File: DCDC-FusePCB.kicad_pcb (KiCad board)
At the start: 2 copper layers, 59 x 39 mm, 11 parts, among them J1 Conn_01x02_Socket, J2 Conn_01x02_Socket

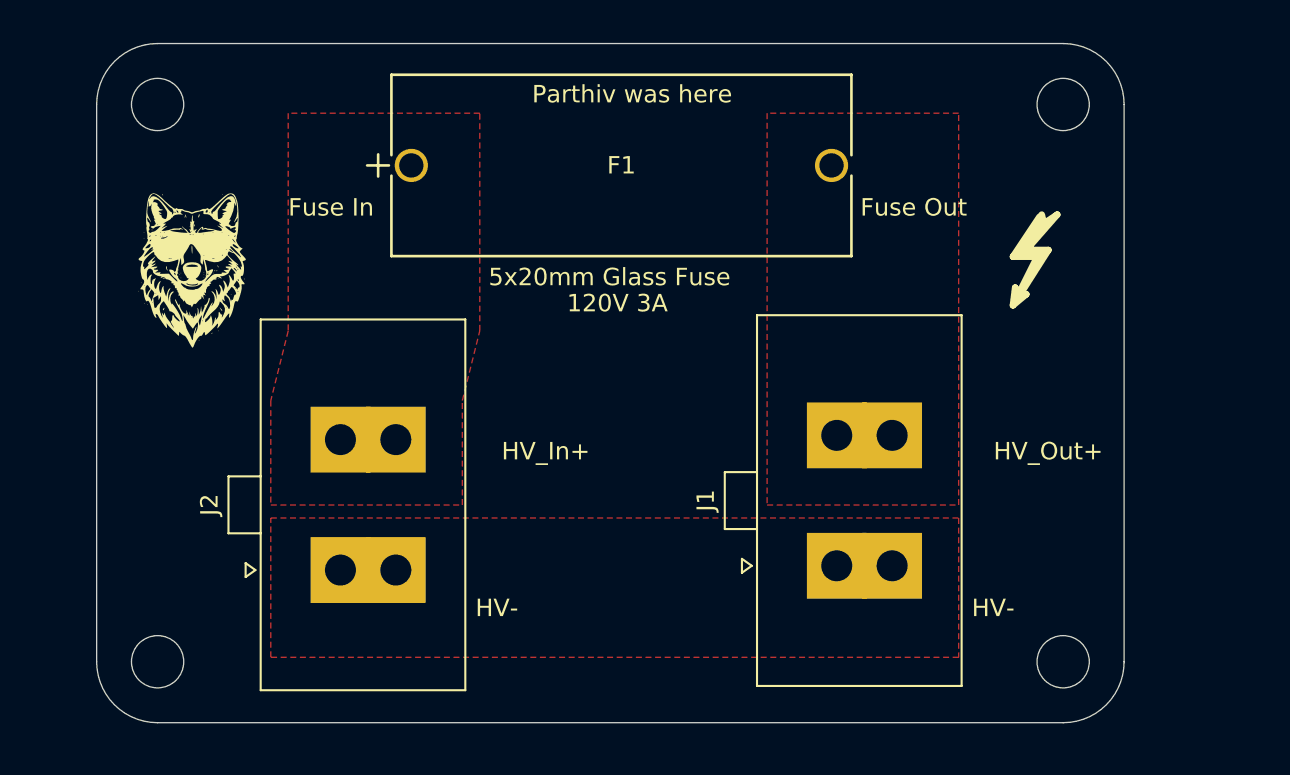
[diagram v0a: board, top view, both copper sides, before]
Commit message: replaced conns with screw terminals
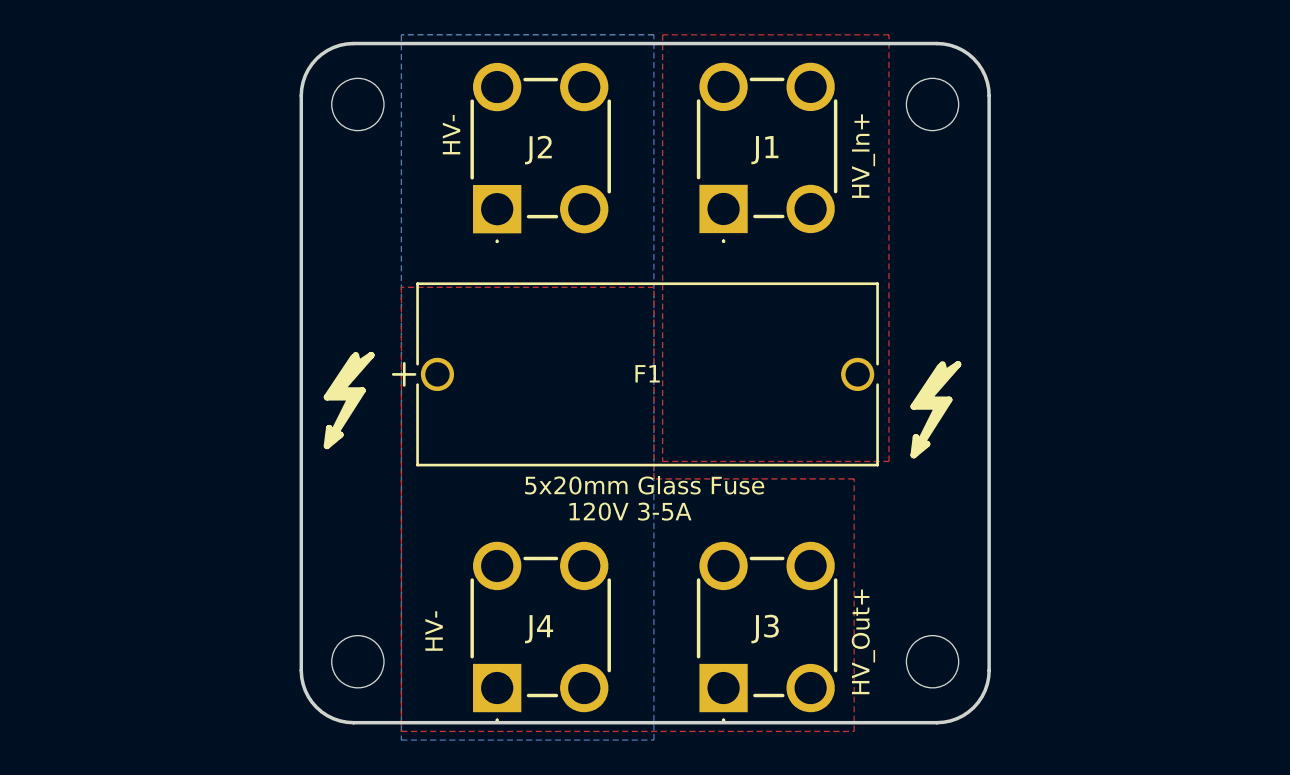
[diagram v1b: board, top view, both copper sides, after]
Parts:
- removed the G*** at (115.0, 80.0)
- added J3: Conn_01x01, CustomFootprints:81915, F.Cu at (145.5, 104.0)
- added J4: Conn_01x01, CustomFootprints:81915, F.Cu at (132.5, 104.0)
- added REF**: Symbol_HighVoltage_Small, UTSVT_Special:Symbol_HighVoltage_Small, F.Cu at (156.8, 88.6)
- J1, J2: value Conn_01x02_Socket -> Conn_01x01; footprint Connector_Molex:Molex_Sabre_43160-0102_1x02_P7.49mm_Vertical -> CustomFootprints:81915
- moved REF** 40.2 mm to (123.1, 88.1)
- moved J1 22.7 mm to (145.5, 76.5), turned to 0 degrees
- moved J2 21.5 mm to (132.5, 76.5), turned to 0 degrees
- moved G*** 20.1 mm to (157.0, 87.0), turned to -90 degrees
- moved F1 12.1 mm to (129.1, 86.0)
- moved REF** 11.5 mm to (124.5, 102.5)
- moved REF** 11.5 mm to (124.5, 70.5)
- moved REF** 7.50 mm to (157.5, 70.5)
- moved REF** 7.50 mm to (157.5, 102.5)
- moved G*** 5.70 mm to (135.5, 86.5)
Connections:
- F1 pad 1: Net-(J2-Pin_2) -> /HV+_Out
- F1 pad 2: Net-(J1-Pin_2) -> /HV+_In
- J1 pad 1: Net-(J1-Pin_1) -> /HV+_In
- J2 pad 1: Net-(J1-Pin_1) -> /HV-
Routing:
- added copper zone on F.Cu, net (none)
- added copper zone on F.Cu, net /HV+_Out
- added copper zone on B.Cu, net /HV-
- removed copper zone on F.Cu, net Net-(J1-Pin_1)
- removed copper zone on F.Cu, net Net-(J1-Pin_2)
- removed copper zone on F.Cu, net Net-(J2-Pin_2)
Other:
- board size 59 x 39 mm -> 39.5 x 39 mm
- board text added: "120V 3-5A"
- board text removed: "120V 3A"
- board text removed: "Fuse In"
- board text removed: "Fuse Out"
- board text removed: "Parthiv was here"

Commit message: mountinghole pads design
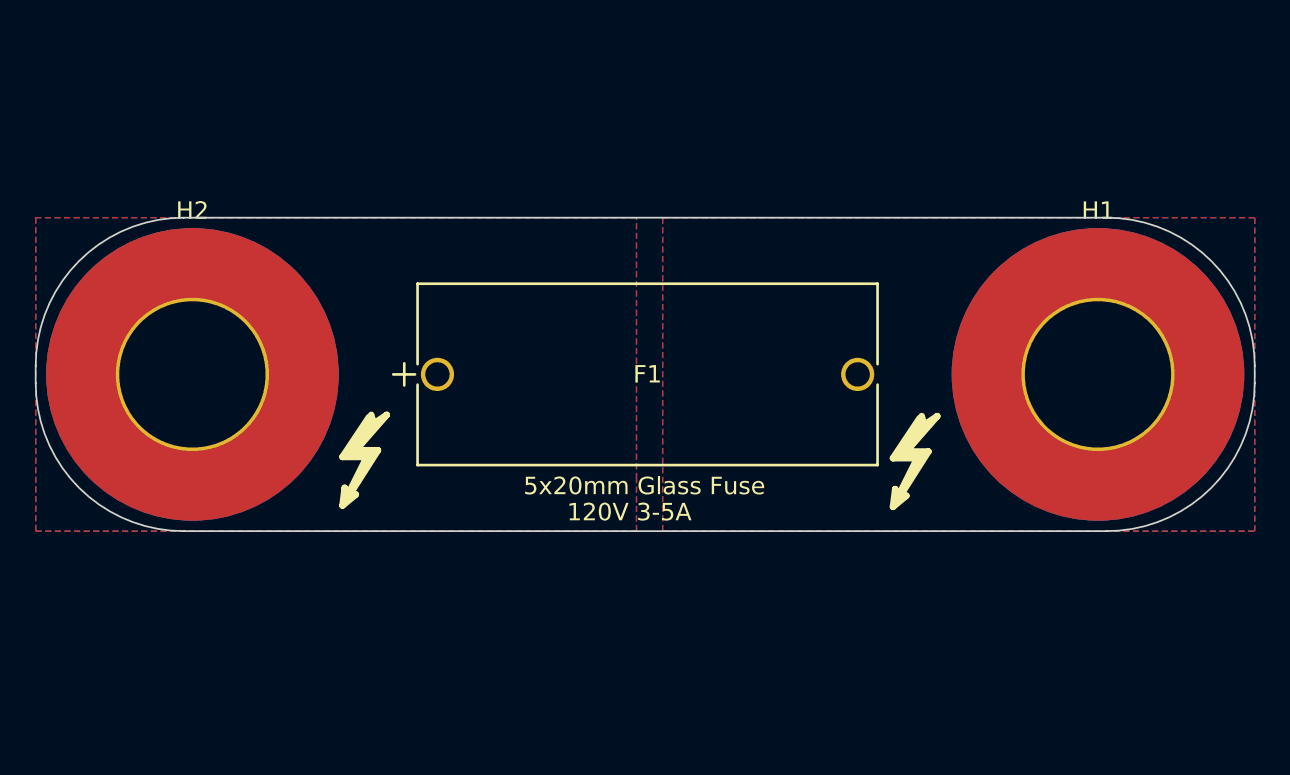
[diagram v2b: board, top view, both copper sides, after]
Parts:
- removed the G*** at (135.5, 86.5)
- removed the G*** at (157.0, 87.0)
- removed J1, J2, J3, J4: Conn_01x01, CustomFootprints:81915
- removed the REF** at (123.1, 88.1)
- removed the REF** at (157.5, 70.5)
- removed the REF** at (124.5, 102.5)
- removed the REF** at (124.5, 70.5)
- removed the REF** at (156.8, 88.6)
- removed the REF** at (157.5, 102.5)
- added G***: LOGO, LOGO, B.Cu at (150.5, 80.0)
- added H1: MountingHole_Pad_MP, MountingHole:MountingHole_8.4mm_M8_Pad_TopBottom, F.Cu at (167.0, 86.0)
- added H2: MountingHole_Pad_MP, MountingHole:MountingHole_8.4mm_M8_Pad_TopBottom, F.Cu at (115.0, 86.0)
- added REF**: Symbol_HighVoltage_Small, UTSVT_Special:Symbol_HighVoltage_Small, F.Cu at (155.6, 91.6)
- added REF**: Symbol_HighVoltage_Small, UTSVT_Special:Symbol_HighVoltage_Small, F.Cu at (124.0, 91.5)
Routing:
- added copper zone on B.Cu, net /HV+_In
- added copper zone on F.Cu, net /HV+_In
- added copper zone on B.Cu, net /HV+_Out
- removed copper zone on F.Cu, net (none)
- removed copper zone on B.Cu, net /HV-
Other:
- board size 39.5 x 39 mm -> 70 x 18 mm
- board text removed: "HV-"
- board text removed: "HV_In+"
- board text removed: "HV_Out+"
